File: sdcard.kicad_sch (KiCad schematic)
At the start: 20 parts, among them J7 microSD push-pull, Q2 -20V 2.3A P-ch, Q3 60V 300mA N-ch

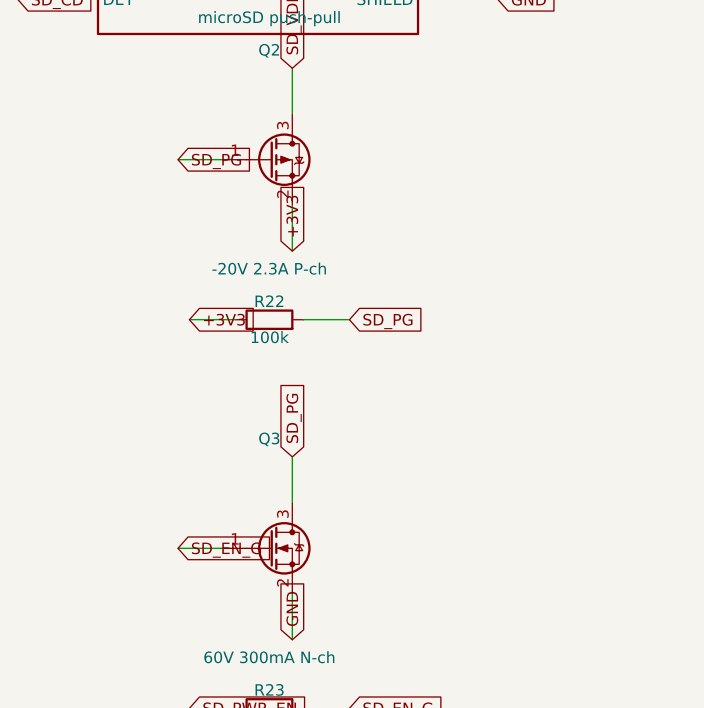
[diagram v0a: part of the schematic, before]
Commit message: Pass ERC clean on KiCad 9.0 and regenerate against its libraries
- Add a PWR_FLAG on VBAT_FB so the LM74700 ANODE power-input pin, fed
  through the reverse-battery FET and EMI bead, no longer trips
  power_pin_not_driven.
- Resolve the generic MOSFET symbols from Transistor_FET where the
  KiCad 9 libraries moved them out of Device.
- Handle the KiCad 9 library format in the raw-symbol extractor: tab
  indentation, CRLF line endings, and no trailing space after the
  symbol name.
- Flatten derived symbols the way KiCad does — carry the child's whole
  property blocks into the parent geometry instead of only swapping the
  value strings — so the embedded USBLC6-2SC6 matches the library copy.
- Regenerate all sheets, netlist, and the PDF plot; embedded symbol
  definitions now come from the KiCad 9.0 (20241209) libraries.

Validated with kicad-cli 9.0: all sheets load, connectivity matches
netlist.txt on 102 nets / 153 instances, ERC clean.

Co-Authored-By: Claude Fable 5 <noreply@anthropic.com>
Claude-Session: https://claude.ai/code/session_01DhNbL25h25p8VFCjRfJik9
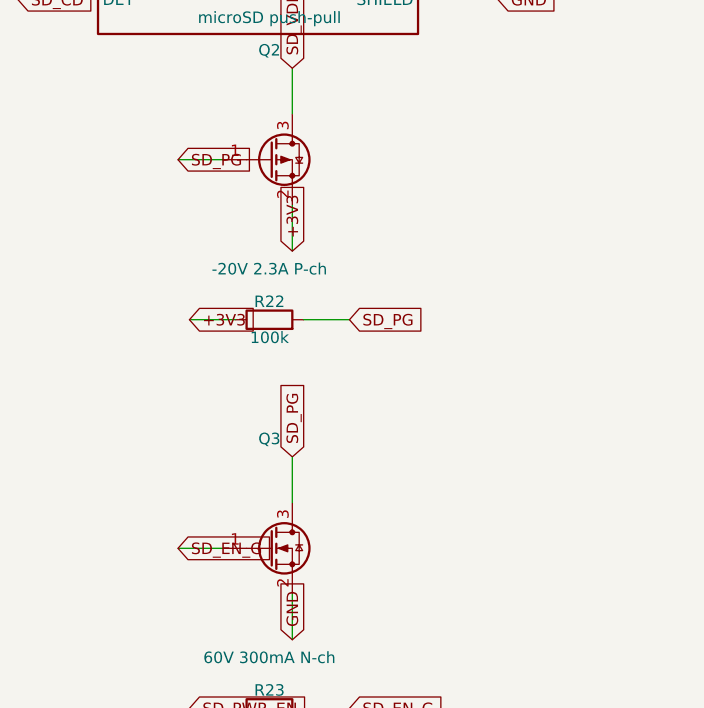
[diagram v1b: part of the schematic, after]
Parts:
- Q2: symbol Device:Q_PMOS_GSD -> Transistor_FET:Q_PMOS_GSD
- Q3: symbol Device:Q_NMOS_GSD -> Transistor_FET:Q_NMOS_GSD

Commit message: Fix the LM5164 power stages against the datasheet and TI's DDA drawing
Review of datasheet SNVSAU4D and package drawing 4214849/B (DDA0008B)
caught five issues, all fixed and re-verified:

- RON placeholders (100k -> ~125/83kHz) corrected to 31.6k (396kHz, 5V)
  and 20.5k (402kHz, 3V3); minimum on-time at the 53.3V clamp is
  237ns/154ns, well above the 50ns floor.
- Bootstrap caps were 100nF; the datasheet mandates exactly 2.2nF and
  warns larger values damage the internal VCC regulator. Now 2.2nF 50V.
- No FB ripple injection on the all-ceramic outputs -- a COT stability
  requirement (Table 6-1). Added Type-3 networks (RA/CA/CB: 121k and
  95.3k / 3.3nF / 270pF) sized for ~20mV ramp at 14V per TI's example.
- Exposed-pad footprint EP2.41x3.3mm was smaller than the DDA0008B pad
  itself (max 2.71x3.4mm); swapped to the EP2.95x4.9mm_Mask2.71x3.4mm
  footprint matching TI's example land pattern.
- Quantified BAT54S back-feed into +3V3: one input shorted to battery
  floats the rail to ~3.6V when the MCU sleeps. Added D2, an MM3Z3V6T1G
  3.6V zener rail clamp.

Load-dump assumption confirmed by the owner: alternator never exceeds
20V, so the SMCJ33A standoff has comfortable margin.

Validated with kicad-cli 9.0: 104 nets / 160 instances match, ERC clean.

Co-Authored-By: Claude Fable 5 <noreply@anthropic.com>
Claude-Session: https://claude.ai/code/session_01DhNbL25h25p8VFCjRfJik9
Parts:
- removed C19: 10uF 6.3V, Capacitor_SMD:C_1206_3216Metric, symbol Device:C
- removed C20: 100nF 16V, Capacitor_SMD:C_0805_2012Metric, symbol Device:C
- removed R22: 100k, Resistor_SMD:R_0805_2012Metric, symbol Device:R
- removed R23: 10k, Resistor_SMD:R_0805_2012Metric, symbol Device:R
- added C23: 10uF 6.3V, Capacitor_SMD:C_1206_3216Metric, symbol Device:C
- added C24: 100nF 16V, Capacitor_SMD:C_0805_2012Metric, symbol Device:C
- added R37, R38: 47k, Resistor_SMD:R_0805_2012Metric, symbol Device:R
- R24: Note (none) -> Default off
- R25: value 33 -> 10k; Note Series damping -> (none)
- R26: value 33 -> 100k; Note Series damping -> (none)
- R31, R32: value 47k -> 33; Note Pulled to the switched rail so nothing back-feeds a powered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 -> Series damping
- R36: Note Card-detect pull-up -> Pulled to the switched rail so nothing back-feeds a powered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
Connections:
- net +3V3: now also R24.1, R38.1; no longer R36.1
- net GND: now also R26.2, C23.2, C24.2; no longer R24.2
- net SD_CD: now also R38.2; no longer R36.2
- net SD_CLK: now also R27.1; no longer R25.1
- net SD_CLK_C: now also R27.2; no longer R25.2
- net SD_CMD: now also R28.1; no longer R26.1
- net SD_CMD_C: now also R28.2, R33.2; no longer R26.2, R31.2
- net SD_D0: now also R29.1; no longer R27.1
- net SD_D0_C: now also R29.2, R34.2; no longer R27.2, R32.2
- net SD_D1: now also R30.1; no longer R28.1
- net SD_D1_C: now also R30.2, R35.2; no longer R28.2, R33.2
- net SD_D2: now also R31.1; no longer R29.1
- net SD_D2_C: now also R31.2, R36.2; no longer R29.2, R34.2
- net SD_D3: now also R32.1; no longer R30.1
- net SD_D3_C: now also R32.2, R37.2; no longer R30.2, R35.2
- net SD_EN_G: now also R25.2, R26.1; no longer R24.1
- net SD_PG: now also R24.2
- net SD_PWR_EN: now also R25.1
- net SD_VDD: now also R36.1, C23.1, C24.1, R37.1; no longer R31.1, R32.1
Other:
- moved on the sheet: R24, R25, R26, R27, R28, R29, R30, R31, R32, R33, R34, R35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
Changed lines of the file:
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@@
   (symbol (lib_id "Device:R") (at 69.85 76.2 90) (unit 1)
     (in_bom yes) (on_board yes) (dnp no)
-    (property "Reference" "R22" (at 69.85 74.2 270)
+    (property "Reference" "R24" (at 69.85 74.2 270)
       (effects (font (size 1.27 1.27)) )
     )
@@
     (instances
       (project "esp32s3-can-sd-logger"
-        (path "/3276c6e6-7085-5954-8442-c6cef7eab316/229b8fda-064c-5815-a4c6-b9c2bb7e623c" (reference "R22") (unit 1))
+        (path "/3276c6e6-7085-5954-8442-c6cef7eab316/229b8fda-064c-5815-a4c6-b9c2bb7e623c" (reference "R24") (unit 1))
       )
     )
@@
   (symbol (lib_id "Device:R") (at 69.85 119.38 90) (unit 1)
     (in_bom yes) (on_board yes) (dnp no)
-    (property "Reference" "R23" (at 69.85 117.38 270)
+    (property "Reference" "R25" (at 69.85 117.38 270)
       (effects (font (size 1.27 1.27)) )
     )
@@
     (instances
       (project "esp32s3-can-sd-logger"
-        (path "/3276c6e6-7085-5954-8442-c6cef7eab316/229b8fda-064c-5815-a4c6-b9c2bb7e623c" (reference "R23") (unit 1))
+        (path "/3276c6e6-7085-5954-8442-c6cef7eab316/229b8fda-064c-5815-a4c6-b9c2bb7e623c" (reference "R25") (unit 1))
       )
     )
@@
   (symbol (lib_id "Device:R") (at 69.85 134.62 90) (unit 1)
     (in_bom yes) (on_board yes) (dnp no)
-    (property "Reference" "R24" (at 69.85 132.62 270)
+    (property "Reference" "R26" (at 69.85 132.62 270)
       (effects (font (size 1.27 1.27)) )
     )
@@
     (instances
       (project "esp32s3-can-sd-logger"
-        (path "/3276c6e6-7085-5954-8442-c6cef7eab316/229b8fda-064c-5815-a4c6-b9c2bb7e623c" (reference "R24") (unit 1))
+        (path "/3276c6e6-7085-5954-8442-c6cef7eab316/229b8fda-064c-5815-a4c6-b9c2bb7e623c" (reference "R26") (unit 1))
       )
     )
@@
   (symbol (lib_id "Device:C") (at 69.85 149.86 90) (unit 1)
     (in_bom yes) (on_board yes) (dnp no)
-    (property "Reference" "C19" (at 69.85 147.86 270)
+    (property "Reference" "C23" (at 69.85 147.86 270)
       (effects (font (size 1.27 1.27)) )
     )
@@
     (instances
       (project "esp32s3-can-sd-logger"
-        (path "/3276c6e6-7085-5954-8442-c6cef7eab316/229b8fda-064c-5815-a4c6-b9c2bb7e623c" (reference "C19") (unit 1))
+        (path "/3276c6e6-7085-5954-8442-c6cef7eab316/229b8fda-064c-5815-a4c6-b9c2bb7e623c" (reference "C23") (unit 1))
       )
     )
@@
   (symbol (lib_id "Device:C") (at 69.85 165.1 90) (unit 1)
     (in_bom yes) (on_board yes) (dnp no)
-    (property "Reference" "C20" (at 69.85 163.1 270)
+    (property "Reference" "C24" (at 69.85 163.1 270)
       (effects (font (size 1.27 1.27)) )
     )
@@
     (instances
       (project "esp32s3-can-sd-logger"
-        (path "/3276c6e6-7085-5954-8442-c6cef7eab316/229b8fda-064c-5815-a4c6-b9c2bb7e623c" (reference "C20") (unit 1))
+        (path "/3276c6e6-7085-5954-8442-c6cef7eab316/229b8fda-064c-5815-a4c6-b9c2bb7e623c" (reference "C24") (unit 1))
       )
     )
@@
   (symbol (lib_id "Device:R") (at 69.85 180.34 90) (unit 1)
     (in_bom yes) (on_board yes) (dnp no)
-    (property "Reference" "R25" (at 69.85 178.34 270)
+    (property "Reference" "R27" (at 69.85 178.34 270)
       (effects (font (size 1.27 1.27)) )
     )
@@
     (instances
       (project "esp32s3-can-sd-logger"
-        (path "/3276c6e6-7085-5954-8442-c6cef7eab316/229b8fda-064c-5815-a4c6-b9c2bb7e623c" (reference "R25") (unit 1))
+        (path "/3276c6e6-7085-5954-8442-c6cef7eab316/229b8fda-064c-5815-a4c6-b9c2bb7e623c" (reference "R27") (unit 1))
       )
     )
@@
   (symbol (lib_id "Device:R") (at 69.85 195.58 90) (unit 1)
     (in_bom yes) (on_board yes) (dnp no)
-    (property "Reference" "R26" (at 69.85 193.58 270)
+    (property "Reference" "R28" (at 69.85 193.58 270)
       (effects (font (size 1.27 1.27)) )
     )
@@
     (instances
       (project "esp32s3-can-sd-logger"
-        (path "/3276c6e6-7085-5954-8442-c6cef7eab316/229b8fda-064c-5815-a4c6-b9c2bb7e623c" (reference "R26") (unit 1))
+        (path "/3276c6e6-7085-5954-8442-c6cef7eab316/229b8fda-064c-5815-a4c6-b9c2bb7e623c" (reference "R28") (unit 1))
       )
     )
@@
   (symbol (lib_id "Device:R") (at 69.85 210.82 90) (unit 1)
     (in_bom yes) (on_board yes) (dnp no)
-    (property "Reference" "R27" (at 69.85 208.82 270)
+    (property "Reference" "R29" (at 69.85 208.82 270)
       (effects (font (size 1.27 1.27)) )
     )
@@
     (instances
       (project "esp32s3-can-sd-logger"
-        (path "/3276c6e6-7085-5954-8442-c6cef7eab316/229b8fda-064c-5815-a4c6-b9c2bb7e623c" (reference "R27") (unit 1))
+        (path "/3276c6e6-7085-5954-8442-c6cef7eab316/229b8fda-064c-5815-a4c6-b9c2bb7e623c" (reference "R29") (unit 1))
       )
     )
@@
   (symbol (lib_id "Device:R") (at 69.85 226.06 90) (unit 1)
     (in_bom yes) (on_board yes) (dnp no)
-    (property "Reference" "R28" (at 69.85 224.06 270)
+    (property "Reference" "R30" (at 69.85 224.06 270)
       (effects (font (size 1.27 1.27)) )
     )
@@
     (instances
       (project "esp32s3-can-sd-logger"
-        (path "/3276c6e6-7085-5954-8442-c6cef7eab316/229b8fda-064c-5815-a4c6-b9c2bb7e623c" (reference "R28") (unit 1))
+        (path "/3276c6e6-7085-5954-8442-c6cef7eab316/229b8fda-064c-5815-a4c6-b9c2bb7e623c" (reference "R30") (unit 1))
       )
     )
@@
   (symbol (lib_id "Device:R") (at 69.85 241.3 90) (unit 1)
     (in_bom yes) (on_board yes) (dnp no)
-    (property "Reference" "R29" (at 69.85 239.3 270)
+    (property "Reference" "R31" (at 69.85 239.3 270)
       (effects (font (size 1.27 1.27)) )
     )
@@
     (instances
       (project "esp32s3-can-sd-logger"
-        (path "/3276c6e6-7085-5954-8442-c6cef7eab316/229b8fda-064c-5815-a4c6-b9c2bb7e623c" (reference "R29") (unit 1))
+        (path "/3276c6e6-7085-5954-8442-c6cef7eab316/229b8fda-064c-5815-a4c6-b9c2bb7e623c" (reference "R31") (unit 1))
       )
     )
@@
   (symbol (lib_id "Device:R") (at 69.85 256.54 90) (unit 1)
     (in_bom yes) (on_board yes) (dnp no)
-    (property "Reference" "R30" (at 69.85 254.54 270)
+    (property "Reference" "R32" (at 69.85 254.54 270)
       (effects (font (size 1.27 1.27)) )
     )
@@
     (instances
       (project "esp32s3-can-sd-logger"
-        (path "/3276c6e6-7085-5954-8442-c6cef7eab316/229b8fda-064c-5815-a4c6-b9c2bb7e623c" (reference "R30") (unit 1))
+        (path "/3276c6e6-7085-5954-8442-c6cef7eab316/229b8fda-064c-5815-a4c6-b9c2bb7e623c" (reference "R32") (unit 1))
       )
     )
@@
   (symbol (lib_id "Device:R") (at 170.18 17.78 90) (unit 1)
     (in_bom yes) (on_board yes) (dnp no)
-    (property "Reference" "R31" (at 170.18 15.78 270)
+    (property "Reference" "R33" (at 170.18 15.78 270)
       (effects (font (size 1.27 1.27)) )
     )
@@
     (instances
       (project "esp32s3-can-sd-logger"
-        (path "/3276c6e6-7085-5954-8442-c6cef7eab316/229b8fda-064c-5815-a4c6-b9c2bb7e623c" (reference "R31") (unit 1))
+        (path "/3276c6e6-7085-5954-8442-c6cef7eab316/229b8fda-064c-5815-a4c6-b9c2bb7e623c" (reference "R33") (unit 1))
       )
     )
@@
   (symbol (lib_id "Device:R") (at 170.18 33.02 90) (unit 1)
     (in_bom yes) (on_board yes) (dnp no)
-    (property "Reference" "R32" (at 170.18 31.02 270)
+    (property "Reference" "R34" (at 170.18 31.02 270)
       (effects (font (size 1.27 1.27)) )
     )
@@
     (instances
       (project "esp32s3-can-sd-logger"
-        (path "/3276c6e6-7085-5954-8442-c6cef7eab316/229b8fda-064c-5815-a4c6-b9c2bb7e623c" (reference "R32") (unit 1))
+        (path "/3276c6e6-7085-5954-8442-c6cef7eab316/229b8fda-064c-5815-a4c6-b9c2bb7e623c" (reference "R34") (unit 1))
       )
     )
@@
   (symbol (lib_id "Device:R") (at 170.18 48.26 90) (unit 1)
     (in_bom yes) (on_board yes) (dnp no)
-    (property "Reference" "R33" (at 170.18 46.26 270)
+    (property "Reference" "R35" (at 170.18 46.26 270)
       (effects (font (size 1.27 1.27)) )
     )
@@
     (instances
       (project "esp32s3-can-sd-logger"
-        (path "/3276c6e6-7085-5954-8442-c6cef7eab316/229b8fda-064c-5815-a4c6-b9c2bb7e623c" (reference "R33") (unit 1))
+        (path "/3276c6e6-7085-5954-8442-c6cef7eab316/229b8fda-064c-5815-a4c6-b9c2bb7e623c" (reference "R35") (unit 1))
       )
     )
@@
   (symbol (lib_id "Device:R") (at 170.18 63.5 90) (unit 1)
     (in_bom yes) (on_board yes) (dnp no)
-    (property "Reference" "R34" (at 170.18 61.5 270)
+    (property "Reference" "R36" (at 170.18 61.5 270)
       (effects (font (size 1.27 1.27)) )
     )
@@
     (instances
       (project "esp32s3-can-sd-logger"
-        (path "/3276c6e6-7085-5954-8442-c6cef7eab316/229b8fda-064c-5815-a4c6-b9c2bb7e623c" (reference "R34") (unit 1))
+        (path "/3276c6e6-7085-5954-8442-c6cef7eab316/229b8fda-064c-5815-a4c6-b9c2bb7e623c" (reference "R36") (unit 1))
       )
     )
@@
   (symbol (lib_id "Device:R") (at 170.18 78.74 90) (unit 1)
     (in_bom yes) (on_board yes) (dnp no)
-    (property "Reference" "R35" (at 170.18 76.74 270)
+    (property "Reference" "R37" (at 170.18 76.74 270)
       (effects (font (size 1.27 1.27)) )
     )
@@
     (instances
       (project "esp32s3-can-sd-logger"
-        (path "/3276c6e6-7085-5954-8442-c6cef7eab316/229b8fda-064c-5815-a4c6-b9c2bb7e623c" (reference "R35") (unit 1))
+        (path "/3276c6e6-7085-5954-8442-c6cef7eab316/229b8fda-064c-5815-a4c6-b9c2bb7e623c" (reference "R37") (unit 1))
       )
     )
@@
   (symbol (lib_id "Device:R") (at 170.18 93.98 90) (unit 1)
     (in_bom yes) (on_board yes) (dnp no)
-    (property "Reference" "R36" (at 170.18 91.98 270)
+    (property "Reference" "R38" (at 170.18 91.98 270)
       (effects (font (size 1.27 1.27)) )
     )
@@
     (instances
       (project "esp32s3-can-sd-logger"
-        (path "/3276c6e6-7085-5954-8442-c6cef7eab316/229b8fda-064c-5815-a4c6-b9c2bb7e623c" (reference "R36") (unit 1))
-      )
-    )
+        (path "/3276c6e6-7085-5954-8442-c6cef7eab316/229b8fda-064c-5815-a4c6-b9c2bb7e623c" (reference "R38") (unit 1))
+      )
+    )
